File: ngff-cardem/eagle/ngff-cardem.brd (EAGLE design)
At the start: 90 x 100 mm, 150 parts, among them IC1 FPF2109, IC2 FPF2109, IC201 CB3Q3244PW, IC202 CB3Q3244PW, IC203 IP4234CZ6, IC3 TPS22958N-DGK, IC302 TPS22958N-DGN, J301 PJ-002BH-SMT-TR, M2 MENTOR_12701001, M3 MENTOR_12701001, Q201 12MHz, T1 BC847, T101 BC847, U201 IP4234CZ6, U202 AT91SAM3S-AU, U301 MIC5366-1.8YC5, X1 PINHD-2X3-SP, X102 ZX360D-B-10P(30), X2 171826-4-RA, X201 MINI-USB-SHIELD-UX60-MB-5ST, X202 2.54mm, X3 JACK2.5_SJ-2523

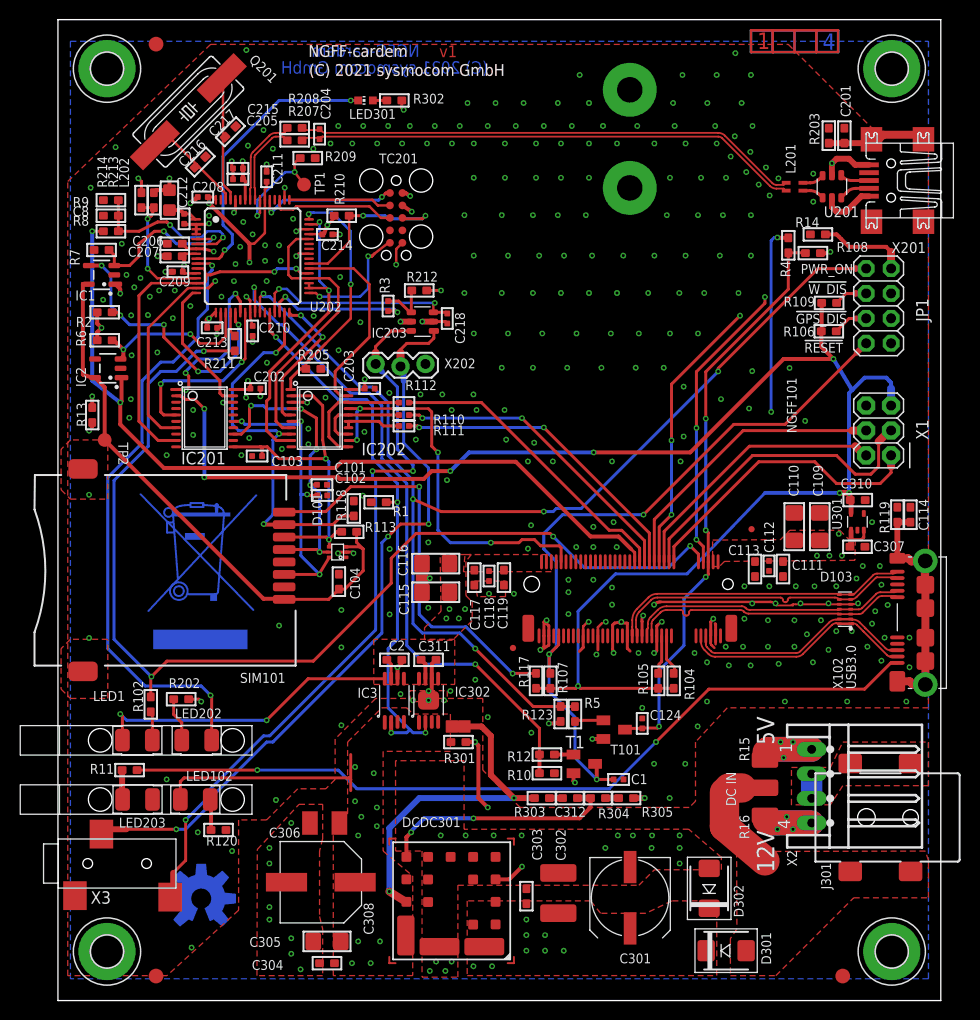
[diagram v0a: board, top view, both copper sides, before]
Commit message: ngff-cardem: run renumber-sheet.uld and normalize-texts2.ulp
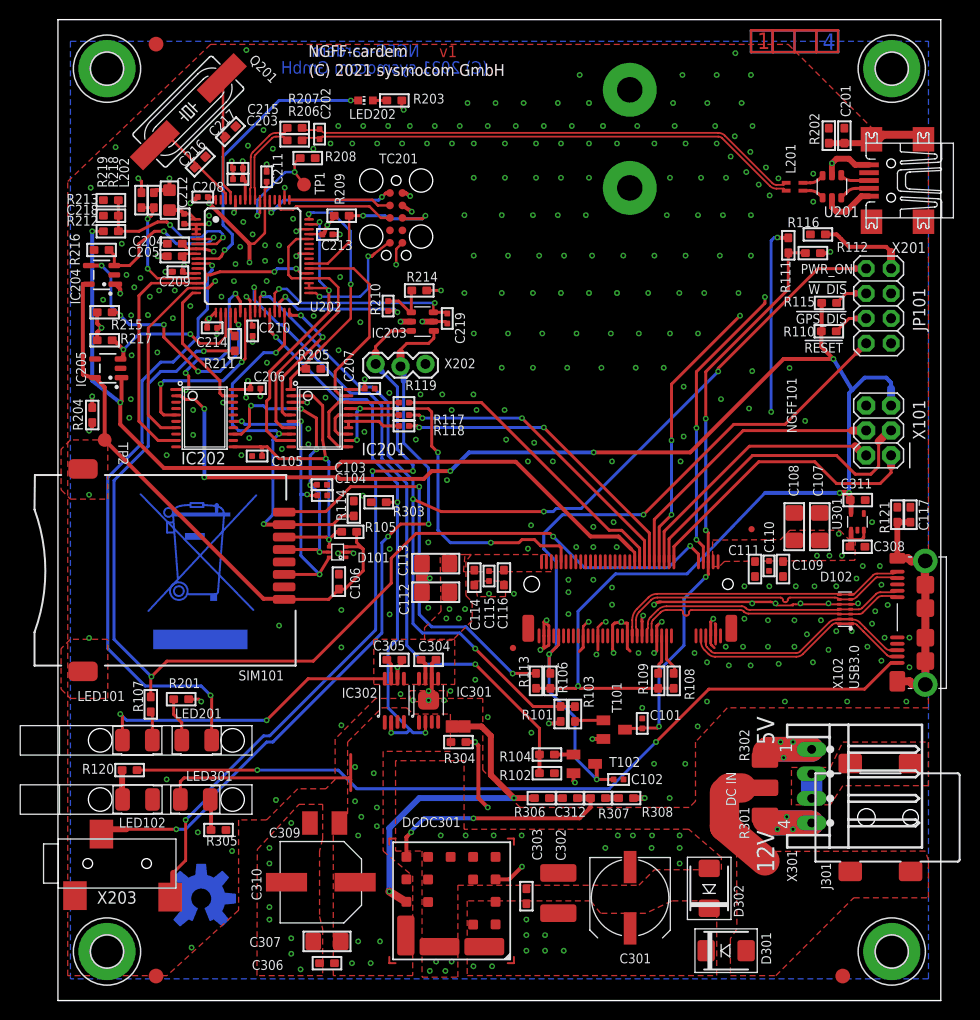
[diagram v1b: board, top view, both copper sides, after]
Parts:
- removed C1, C118, C124: 33p, rc-sysmocom:_0402
- removed C119: 10p, rc-sysmocom:_0603
- removed C2: 1n, rc-sysmocom:_0603
- removed C8, R10: DNP, rc-sysmocom:_0603
- removed H1, H2: MOUNT-PAD-ROUND3.2, holes:3,2-PAD
- removed IC3: TPS22958N-DGK, TPS22958:VSSOP8
- removed JP1: (no value), pinhead:2X04
- removed LED203: LEDPLCC2-MIN-red, LED-PLCC2:PLCC2-MIN
- removed R1, R4: 10k, rc-sysmocom:_0603
- removed R11: 510, rc-sysmocom:_0603
- removed R12: 4.7k, rc-sysmocom:_0603
- removed R15, R16: 0R, rc-sysmocom:1210
- removed R3: 47, rc-sysmocom:_0402
- removed R8: 30k, rc-sysmocom:_0603
- removed R9: 47k, rc-sysmocom:_0603
- added C105, C219: 33p, rc-sysmocom:_0402
- added C106: 100n, rc-sysmocom:_0603
- added C107, C108: 100u, rc-sysmocom:1206
- added C309: DNP, rcl:SMC_B
- added H301, H302: MOUNT-PAD-ROUND3.2, holes:3,2-PAD
- added IC301: TPS22958N-DGN, TPS22958:HVSSOP8
- added JP103: FIDUCIALUFIDUCIAL, SparkFun:MICRO-FIDUCIAL
- added LED201: LEDPLCC2-MIN-red, LED-PLCC2:PLCC2-MIN
- added R114: 47k, rc-sysmocom:_0603
- added R115, R218: 10k, rc-sysmocom:_0603
- added R121, R219: 100k, rc-sysmocom:_0603
- added R201: 330, rc-sysmocom:_0603
- added R206: 27, rc-sysmocom:_0603
- added R306: 180, rc-sysmocom:_0603
- added R307: 4.42k, rc-sysmocom:_0603
- added R308: 20, rc-sysmocom:_0603
- C104: value 100n -> 33p; device rc-sysmocom:_0603 -> rc-sysmocom:_0402
- C109: value 100u -> 100n; device rc-sysmocom:1206 -> rc-sysmocom:_0603
- C110, C115: value 100u -> 33p; device rc-sysmocom:1206 -> rc-sysmocom:_0402
- C111: value 100n -> 10p
- C112: value 33p -> 100u; device rc-sysmocom:_0402 -> rc-sysmocom:1206
- C113: value 10p -> 100u; device rc-sysmocom:_0603 -> rc-sysmocom:1206
- C116: value 100u -> 10p; device rc-sysmocom:1206 -> rc-sysmocom:_0603
- C202: value 100n -> 33p
- C204: value 33p -> 2.2u; device rc-sysmocom:_0402 -> rc-sysmocom:_0603
- C205: value 100n -> 2.2u; device rc-sysmocom:_0402 -> rc-sysmocom:_0603
- C206, C207: value 2.2u -> 100n; device rc-sysmocom:_0603 -> rc-sysmocom:_0402
- C218: value 33p -> DNP; device rc-sysmocom:_0402 -> rc-sysmocom:_0603
- C304: value 100n -> 1n
- C305: value 22u 10V -> 1n; device rc-sysmocom:1206 -> rc-sysmocom:_0603
- C306: value DNP -> 100n; device rcl:SMC_B -> rc-sysmocom:_0603
- C307: value 100n -> 22u 10V; device rc-sysmocom:_0603 -> rc-sysmocom:1206
- C308: value 330u -> 100n; device Wurth_Elektronik_Passive_Capacitors_rev15a:4.2X1.9X2.8(BXCXA) -> rc-sysmocom:_0603
- C310: value 100n -> 330u; device rc-sysmocom:_0603 -> Wurth_Elektronik_Passive_Capacitors_rev15a:4.2X1.9X2.8(BXCXA)
- C311: value 1n -> 100n
- IC302: value TPS22958N-DGN -> TPS22958N-DGK; device TPS22958:HVSSOP8 -> TPS22958:VSSOP8
- JP101: value FIDUCIALUFIDUCIAL -> (none); device SparkFun:MICRO-FIDUCIAL -> pinhead:2X04
- LED102: value LEDPLCC2-MIN -> LEDPLCC2-MIN-red
- LED202: value LEDPLCC2-MIN-red -> KPH-1608SGC; device LED-PLCC2:PLCC2-MIN -> led:CHIP-LED0603
- LED301: value KPH-1608SGC -> LEDPLCC2-MIN; device led:CHIP-LED0603 -> LED-PLCC2:PLCC2-MIN
- R102: value 330 -> DNP
- R104: value 10k -> 4.7k
- R105: value 10k -> DNP
- R107: value 10k -> 330
- R108: value 100k -> 10k
- R110, R111: value 47 -> 10k; device rc-sysmocom:_0402 -> rc-sysmocom:_0603
- R112: value 47 -> 100k; device rc-sysmocom:_0402 -> rc-sysmocom:_0603
- R113: value DNP -> 4.7k
- R117: value 4.7k -> 47; device rc-sysmocom:_0603 -> rc-sysmocom:_0402
- R118: value 47k -> 47; device rc-sysmocom:_0603 -> rc-sysmocom:_0402
- R119: value 100k -> 47; device rc-sysmocom:_0603 -> rc-sysmocom:_0402
- R120: value 330 -> 510
- R202: value 330 -> 100k
- R203: value 100k -> 330
- R208: value 27 -> 10k
- R209: value 10k -> 1.5k
- R210: value 1.5k -> 47; device rc-sysmocom:_0603 -> rc-sysmocom:_0402
- R212: value 100k -> 30k
- R213: value 10k -> 47k
- R301: value 100k -> 0R; device rc-sysmocom:_0603 -> rc-sysmocom:1210
- R302: value 330 -> 0R; device rc-sysmocom:_0603 -> rc-sysmocom:1210
- R303: value 180 -> 10k
- R304: value 4.42k -> 100k
- R305: value 20 -> 330
- moved H303 90.0 mm to (5.00, 5.00)
- moved H304 90.0 mm to (85.0, 5.00)
- moved R202 87.5 mm to (78.6, 88.2), turned to 90 degrees
- moved R302 78.3 mm to (72.1, 23.1), turned to 90 degrees
- moved LED301 73.3 mm to (14.0, 20.5), turned to 0 degrees
- moved LED202 67.4 mm to (31.4, 91.8), turned to 90 degrees
- moved C307 67.4 mm to (27.4, 6.03)
- moved C310 67.2 mm to (26.8, 12.1), turned to 0 degrees
- moved C308 64.5 mm to (81.5, 46.3), turned to 180 degrees
- moved R119 51.6 mm to (35.3, 61.0), turned to 180 degrees
- moved JP101 51.0 mm to (83.7, 70.8), turned to 270 degrees
- moved C311 46.7 mm to (81.5, 51.0)
- moved R108 45.9 mm to (62.8, 32.6), turned to 270 degrees
- moved R106 45.6 mm to (50.2, 32.6), turned to 270 degrees
- moved C114 44.9 mm to (42.4, 43.1), turned to 90 degrees
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- renumbered D103 to D102, IC1 to IC204, IC2 to IC205, LED1 to LED101, R123 to R101, R13 to R204, R14 to R116, R2 to R215, R5 to R103, R6 to R217, R7 to R216, T1 to T102, X1 to X101, X2 to X301, X3 to X203
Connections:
- net !BODY_SAR: now also R109.1; no longer R105.1
- net !CONNECT_MDM_SIM: now also IC201.1; no longer IC202.1
- net !CONNECT_UART1: now also IC202.19; no longer IC201.19
- net !CONNECT_UART2: now also IC201.19; no longer IC202.19
- net !GPS_DISABLE: now also JP101.5, R110.1; no longer JP1.5, R106.1
- net !MDM_UIM_RST: now also IC201.14, IC201.15, R118.2; no longer IC202.14, IC202.15, R111.2
- net !NGFF_RESET: now also C102.1, JP101.7, R106.1; no longer C1.1, JP1.7, R107.1
- net !PWR_ON: now also JP101.1; no longer JP1.1
- net !SET_SIM_DET: now also IC202.1; no longer IC201.1
- net !SIMTRACE_RESET: now also R209.1; no longer R210.1
- net !SLOT_RST: now also C104.1, IC201.6, IC202.15; no longer C102.1, IC201.15, IC202.6
- net !ST_UART1_RST: now also IC202.5; no longer IC201.5
- net !ST_UART2_RST: now also IC201.5; no longer IC202.5
- net !WAKE_ON_WWAN: now also R108.1; no longer R104.1
- net !W_DISABLE: now also JP101.3, R115.1; no longer JP1.3, R109.1
- net +VIN: now also R301.2, R302.1; no longer R15.1, R16.2
- net ERASE: now also R208.2; no longer R209.2
- net GND: now also C105.2, C106.2, C107.1, C108.1, C110.2, C111.2, C112.1, C113.1, C115.2, C116.2, C204.1, C219.2, C305.1, C306.1, C307.2, C308.1, C309.-, C310.2, H301.B3,2, H302.B3,2, IC301.6, IC301.EXP, JP101.4, JP101.6, JP101.8, LED102.K, R102.2, R112.1, R114.1, R121.1, R202.2, R208.1, R213.1, R219.1, R303.1, R305.1, R308.2; no longer C1.2, C110.1, C111.1, C112.2, C113.2, C115.1, C116.1, C118.2, C119.2, C124.2, C2.1, C202.1, C305.2, C306.-, C307.1, C308.2, C310.1, C8.2, H1.B3,2, H2.B3,2, IC3.6, IC302.EXP, JP1.4, JP1.6, JP1.8, LED203.K, R1.1, R10.2, R108.1, R118.1, R119.1, R120.1, R203.2, R209.1, R214.1, R305.2, R9.1
- net MDM_SIM_DET: now also IC201.12, IC201.17; no longer IC202.12, IC202.17
- net MDM_UIM_CLK: now also IC201.13, IC201.16, R117.2; no longer IC202.13, IC202.16, R110.2
- net MDM_UIM_IO: now also IC201.11, IC201.18, R119.2; no longer IC202.11, IC202.18, R112.2
- net MDM_UIM_VDD: now also R212.2; no longer R8.2
- net MODEM_EN: now also IC301.2, R303.2; no longer IC3.2, R1.2
- net N$10: now also C117.2, R121.2; no longer C114.2, R119.2
- net N$11: now also R104.1; no longer R12.1
- net N$12: now also LED201.A, R201.1; no longer LED202.A, R202.1
- net N$13: now also R304.2; no longer R301.2
- net N$18: now also C218.1, R212.1, R213.2; no longer C8.1, R8.1, R9.2
- net N$19: now also LED102.A, R120.1; no longer LED203.A, R11.1
- net N$20: now also C305.2, IC302.7; no longer C2.2, IC3.7
- net N$21: now also JP101.2; no longer JP1.2
- net N$22: now also R107.1; no longer R102.1
- net N$23: now also R301.1; no longer R16.1
- net N$24: now also R302.2; no longer R15.2
- net N$3: now also R113.2; no longer R117.2
- net N$4: now also LED202.A, R203.2; no longer LED301.A, R302.2
- net N$5: now also IC201.3, IC202.18; no longer IC201.18, IC202.3
- net N$59: now also R307.2, R308.1; no longer R304.2, R305.1
- net N$6: now also R306.2; no longer R303.2
- net N$7: now also LED301.K, R305.2; no longer LED102.K, R120.2
- net N$8: now also R210.1; no longer R3.1
- net N$9: now also R202.1; no longer R203.1
- net N$91: now also C304.2, IC301.7; no longer C311.2, IC302.7
- net NGFF_USB_VBUS: now also R120.2; no longer R11.2
- net PERST: now also R102.1, R104.2; no longer R10.1, R12.2
- net PWR_ON: now also C101.1, R111.2, R112.2; no longer C124.1, R108.2, R4.2
- net SENSE: now also R306.1; no longer R303.1
- net SIMTRACE12_USB_D_N: now also C202.1, R206.1; no longer C204.1, R207.1
- net SIMTRACE12_USB_D_P: now also C202.2, R207.1; no longer C204.2, R208.1
- net SIMTRACE_LED_GREEN: now also LED201.K; no longer LED202.K
- net SIMTRACE_LED_RED: now also LED202.C; no longer LED301.C
- net SLOT_CLK: now also C103.1, IC201.4, IC202.13; no longer C101.1, IC201.13, IC202.4
- net SLOT_DET: now also IC201.8, R114.2; no longer IC202.8, R118.2
- net SLOT_IO: now also C105.1, IC201.2, IC202.11, R105.2; no longer C103.1, IC201.11, IC202.2, R113.2
- net SLOT_VDD: now also C106.1, R105.1; no longer C104.1, R113.1
- net ST_DRXD: now also R210.2, R214.1; no longer R212.1, R3.2
- net ST_DTXD: now also C219.1; no longer C218.1
- net ST_UART1_CLK: now also IC202.7; no longer IC201.7
- net ST_UART1_IO: now also IC202.9; no longer IC201.9
- net ST_UART2_CLK: now also IC201.7; no longer IC202.7
- net ST_UART2_IO: now also IC201.9; no longer IC202.9
- net TRIM: now also R307.1; no longer R304.1
- net VCC_1V8: now also C311.2, IC202.2, R108.2, R110.2, R113.1, R115.2; no longer C310.2, IC201.2, R104.2, R105.2, R107.2, R117.1
- net VCC_3V3: now also C204.2, C207.2, C306.2, C307.1, C309.+, C310.1, IC301.1, IC301.3, IC301.4, LED301.A, R201.2, R203.1, R209.2, R214.2, R218.1, R304.1; no longer C202.2, C205.2, C304.2, C305.1, C306.+, C308.1, IC3.1, IC3.3, IC3.4, LED102.A, R202.2, R210.2, R212.2, R213.1, R301.1, R302.1
- net VDD_1V8_SIMTRACE12: now also C205.2; no longer C207.2
- net VERSION_DETECT: now also R218.2, R219.2; no longer R213.2, R214.2
- net V_MODEM: now also C107.2, C108.2, C110.1, C111.1, C112.2, C113.2, C114.2, C115.1, C116.1, C308.2, IC301.5, IC301.8, R111.1; no longer C110.2, C111.2, C112.1, C113.1, C115.2, C116.2, C117.2, C118.1, C119.1, C307.2, IC3.5, IC3.8, R4.1
- net WWAN: now also R107.2; no longer R102.2
- net _!USIM1_RESET: now also R118.1; no longer R111.1
- net _SIMTRACE12_USB_D_N: now also R206.2; no longer R207.2
- net _SIMTRACE12_USB_D_P: now also R207.2; no longer R208.2
- net _USIM1_CLK: now also R117.1; no longer R110.1
- net _USIM1_DATA: now also R119.1; no longer R112.1

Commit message: ngff-cardem: update parts for BOM (in gnumeric and xls)
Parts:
- C312: value 3300p -> 8200p
- LED102, LED201: value LEDPLCC2-MIN-red -> LEDPLCC2-MIN-green
- LED202: value KPH-1608SGC -> KPH-1608EC
- LED301: value LEDPLCC2-MIN -> LEDPLCC2-MIN-green
- R302: value 0R -> DNP

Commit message: ngff-cardem: make DCDC301 default to Murata OKL-T/3-W12P-C
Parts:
- DCDC301: value PVX003A0X3-SRZ -> OKL-T/3-W12P-C
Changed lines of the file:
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@@
 <attribute name="VALUE" x="9.7165" y="83.5024" size="0.508" layer="27" font="vector" ratio="10" rot="R270"/>
 </element>
-<element name="DCDC301" library="DC-DC_CONVERTER" package="DC-DC_CON-ALLPADS" value="PVX003A0X3-SRZ" x="40.1325" y="10.165" smashed="yes" rot="R180">
+<element name="DCDC301" library="DC-DC_CONVERTER" package="DC-DC_CON-ALLPADS" value="OKL-T/3-W12P-C" x="40.1325" y="10.165" smashed="yes" rot="R180">
 <attribute name="NAME" x="41.0525" y="18.6875" size="1" layer="25" ratio="16" rot="R180"/>
-<attribute name="DESCRIPTION" value="DC DC CONVERTER 0.6-5.5V 16.5W" x="40.1325" y="10.165" size="1.778" layer="27" rot="R180" display="off"/>
-<attribute name="MANUFACTURER" value="ABB Power Electronics Inc." x="40.1325" y="10.165" size="1.778" layer="27" rot="R180" display="off"/>
-<attribute name="MANUFACTURERPARTNUMBER" value="PVX003A0X3-SRZ" x="40.1325" y="10.165" size="1.778" layer="27" rot="R180" display="off"/>
+<attribute name="DESCRIPTION" value="DC DC CONVERTER 0.591-5.5V 15W" x="40.1325" y="10.165" size="1.778" layer="27" rot="R180" display="off"/>
+<attribute name="MANUFACTURER" value="Murata Power Solutions Inc." x="40.1325" y="10.165" size="1.778" layer="27" rot="R180" display="off"/>
+<attribute name="MANUFACTURERPARTNUMBER" value="OKL-T/3-W12P-C" x="40.1325" y="10.165" size="1.778" layer="27" rot="R180" display="off"/>
 <attribute name="SOURCE" value="DIGIKEY" x="40.1325" y="10.165" size="1.778" layer="27" rot="R180" display="off"/>
-<attribute name="SOURCEPARTNUMBER" value="555-1264-1-ND" x="40.1325" y="10.165" size="1.778" layer="27" rot="R180" display="off"/>
+<attribute name="SOURCEPARTNUMBER" value="811-2709-1-ND" x="40.1325" y="10.165" size="1.778" layer="27" rot="R180" display="off"/>
 <attribute name="ROHSCERTIFICATE" value="RoHS-konform" x="40.1325" y="10.165" size="1.778" layer="27" rot="R180" display="off"/>
 <attribute name="POPULATED" value="TRUE" x="40.1325" y="10.165" size="1.778" layer="27" rot="R180" display="off"/>
 <attribute name="CLASS" value="DC/DC CONVERTER" x="40.1325" y="10.165" size="1.778" layer="27" rot="R180" display="off"/>
-<attribute name="LINK" value="https://www.digikey.de/product-detail/de/abb-power-electronics-inc/PVX003A0X3-SRZ/555-1264-1-ND" x="40.1325" y="10.165" size="1.778" layer="27" rot="R180" display="off"/>
+<attribute name="LINK" value="https://www.digikey.de/product-detail/de/murata-power-solutions-inc/OKL-T-3-W12P-C/811-2709-1-ND" x="40.1325" y="10.165" size="1.778" layer="27" rot="R180" display="off"/>
 </element>
 <element name="R304" library="rc-sysmocom" package="_0603" value="100k" x="40.825" y="26.3525" smashed="yes">

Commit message: ngff-cardem: exchange two BJT to available types (BC850)
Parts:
- T101, T102: value BC847 -> BC850
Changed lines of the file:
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@@
 <attribute name="LINK" value="https://www.digikey.de/product-detail/de/te-connectivity-passive-product/CRG0603F10K-10/A121523CT-ND/" x="18.035" y="66.9925" size="1.778" layer="27" rot="R90" display="off"/>
 </element>
-<element name="T101" library="transistor" package="SOT23-BEC" value="BC847" x="56.705" y="27.6175" smashed="yes" rot="R270">
+<element name="T101" library="transistor" package="SOT23-BEC" value="BC850" x="56.705" y="27.6175" smashed="yes" rot="R270">
 <attribute name="NAME" x="57.4625" y="29.3375" size="1" layer="25" ratio="16" rot="R90"/>
 <attribute name="VALUE" x="53.53" y="29.5225" size="1.27" layer="27" rot="R270"/>
-<attribute name="DESCRIPTION" value="TRANS NPN 45V 0.1A SOT23" x="56.705" y="27.6175" size="1.778" layer="27" rot="R270" display="off"/>
+<attribute name="DESCRIPTION" value="TRANS NPN 45V 100MA TO236AB" x="56.705" y="27.6175" size="1.778" layer="27" rot="R270" display="off"/>
 <attribute name="MANUFACTURER" value="Nexperia USA Inc." x="56.705" y="27.6175" size="1.778" layer="27" rot="R270" display="off"/>
-<attribute name="MANUFACTURERPARTNUMBER" value="BC847C,215" x="56.705" y="27.6175" size="1.778" layer="27" rot="R270" display="off"/>
+<attribute name="MANUFACTURERPARTNUMBER" value="BC850C,235" x="56.705" y="27.6175" size="1.778" layer="27" rot="R270" display="off"/>
 <attribute name="SOURCE" value="DIGIKEY" x="56.705" y="27.6175" size="1.778" layer="27" rot="R270" display="off"/>
-<attribute name="SOURCEPARTNUMBER" value="1727-2924-1-ND" x="56.705" y="27.6175" size="1.778" layer="27" rot="R270" display="off"/>
+<attribute name="SOURCEPARTNUMBER" value="1727-6194-1-ND" x="56.705" y="27.6175" size="1.778" layer="27" rot="R270" display="off"/>
 <attribute name="ROHSCERTIFICATE" value="RoHS3-konform" x="56.705" y="27.6175" size="1.778" layer="27" rot="R270" display="off"/>
 <attribute name="POPULATED" value="TRUE" x="56.705" y="27.6175" size="1.778" layer="27" rot="R270" display="off"/>
 <attribute name="CLASS" value="TRANSISTOR" x="56.705" y="27.6175" size="1.778" layer="27" rot="R270" display="off"/>
-<attribute name="LINK" value="https://www.digikey.de/product-detail/de/nexperia-usa-inc/BC847C,215/1727-2924-1-ND" x="56.705" y="27.6175" size="1.778" layer="27" rot="R270" display="off"/>
+<attribute name="LINK" value="https://www.digikey.de/product-detail/de/nexperia-usa-inc/BC850C-235/1727-6194-1-ND/" x="56.705" y="27.6175" size="1.778" layer="27" rot="R270" display="off"/>
 </element>
 <element name="C101" library="rc-sysmocom" package="_0402" value="33p" x="59.5625" y="28.2525" smashed="yes" rot="R90">
@@
 <attribute name="VALUE" x="34.9886" y="69.5325" size="0.508" layer="27" font="vector" ratio="10" rot="R90"/>
 </element>
-<element name="T102" library="transistor" package="SOT23-BEC" value="BC847" x="53.6575" y="24.13" smashed="yes" rot="R270">
-<attribute name="SOURCEPARTNUMBER" value="1727-2924-1-ND" x="53.6575" y="24.13" size="1.016" layer="27" ratio="14" rot="R270" display="off"/>
-<attribute name="DESCRIPTION" value="TRANS NPN 45V 0.1A SOT23" x="53.6575" y="24.13" size="1.016" layer="27" ratio="14" rot="R270" display="off"/>
-<attribute name="CLASS" value="TRANSISTOR" x="53.6575" y="24.13" size="1.016" layer="27" ratio="14" rot="R270" display="off"/>
-<attribute name="SOURCE" value="DIGIKEY" x="53.6575" y="24.13" size="1.016" layer="27" ratio="14" rot="R270" display="off"/>
-<attribute name="LINK" value="https://www.digikey.de/product-detail/de/nexperia-usa-inc/BC847C,215/1727-2924-1-ND" x="53.6575" y="24.13" size="1.016" layer="27" ratio="14" rot="R270" display="off"/>
-<attribute name="MANUFACTURER" value="Nexperia USA Inc." x="53.6575" y="24.13" size="1.016" layer="27" ratio="14" rot="R270" display="off"/>
-<attribute name="MANUFACTURERPARTNUMBER" value="BC847C,215" x="53.6575" y="24.13" size="1.016" layer="27" ratio="14" rot="R270" display="off"/>
-<attribute name="POPULATED" value="TRUE" x="53.6575" y="24.13" size="1.016" layer="27" ratio="14" rot="R270" display="off"/>
-<attribute name="ROHSCERTIFICATE" value="RoHS3-konform" x="53.6575" y="24.13" size="1.016" layer="27" ratio="14" rot="R270" display="off"/>
+<element name="T102" library="transistor" package="SOT23-BEC" value="BC850" x="53.6575" y="24.13" smashed="yes" rot="R270">
 <attribute name="NAME" x="56.1975" y="23.8125" size="1.016" layer="25" ratio="14"/>
 <attribute name="VALUE" x="50.4825" y="26.035" size="1.27" layer="27" rot="R270"/>
+<attribute name="DESCRIPTION" value="TRANS NPN 45V 100MA TO236AB" x="53.6575" y="24.13" size="1.778" layer="27" rot="R270" display="off"/>
+<attribute name="MANUFACTURER" value="Nexperia USA Inc." x="53.6575" y="24.13" size="1.778" layer="27" rot="R270" display="off"/>
+<attribute name="MANUFACTURERPARTNUMBER" value="BC850C,235" x="53.6575" y="24.13" size="1.778" layer="27" rot="R270" display="off"/>
+<attribute name="SOURCE" value="DIGIKEY" x="53.6575" y="24.13" size="1.778" layer="27" rot="R270" display="off"/>
+<attribute name="SOURCEPARTNUMBER" value="1727-6194-1-ND" x="53.6575" y="24.13" size="1.778" layer="27" rot="R270" display="off"/>
+<attribute name="ROHSCERTIFICATE" value="RoHS3-konform" x="53.6575" y="24.13" size="1.778" layer="27" rot="R270" display="off"/>
+<attribute name="POPULATED" value="TRUE" x="53.6575" y="24.13" size="1.778" layer="27" rot="R270" display="off"/>
+<attribute name="CLASS" value="TRANSISTOR" x="53.6575" y="24.13" size="1.778" layer="27" rot="R270" display="off"/>
+<attribute name="LINK" value="https://www.digikey.de/product-detail/de/nexperia-usa-inc/BC850C-235/1727-6194-1-ND/" x="53.6575" y="24.13" size="1.778" layer="27" rot="R270" display="off"/>
 </element>
 <element name="C102" library="rc-sysmocom" package="_0402" value="33p" x="57.15" y="22.5425" smashed="yes">

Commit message: ngff-cardem: populate R102 to uncond' release /NGFF_RESET (solves SYS#5531)
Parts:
- R102: value DNP -> 10k
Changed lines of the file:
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@@
 <attribute name="VALUE" x="55.88" y="21.2089" size="0.508" layer="27" font="vector" ratio="10"/>
 </element>
-<element name="R102" library="rc-sysmocom" package="_0603" value="DNP" x="49.8475" y="23.1775" smashed="yes">
+<element name="R102" library="rc-sysmocom" package="_0603" value="10k" x="49.8475" y="23.1775" smashed="yes">
 <attribute name="NAME" x="48.26" y="23.495" size="1.016" layer="25" font="vector" ratio="14" rot="R180"/>
 <attribute name="VALUE" x="48.26" y="21.6852" size="0.508" layer="27" font="vector" ratio="10"/>
-<attribute name="DESCRIPTION" value="NO DESCRIPTION" x="49.8475" y="23.1775" size="1.778" layer="27" display="off"/>
-<attribute name="MANUFACTURER" value="UNKNOWN MANUFACTURER" x="49.8475" y="23.1775" size="1.778" layer="27" display="off"/>
-<attribute name="MANUFACTURERPARTNUMBER" value="UNKNOWN MANUFACTURER PART NUMBER" x="49.8475" y="23.1775" size="1.778" layer="27" display="off"/>
-<attribute name="SOURCE" value="UNKNOWN SOURCE" x="49.8475" y="23.1775" size="1.778" layer="27" display="off"/>
-<attribute name="SOURCEPARTNUMBER" value="UNKNOWN SOURCE PART NUMBER" x="49.8475" y="23.1775" size="1.778" layer="27" display="off"/>
-<attribute name="ROHSCERTIFICATE" value="UNKNOWN ROHS CERTIFICATE" x="49.8475" y="23.1775" size="1.778" layer="27" display="off"/>
-<attribute name="POPULATED" value="FALSE" x="49.8475" y="23.1775" size="1.778" layer="27" display="off"/>
+<attribute name="DESCRIPTION" value="RES SMD 10K OHM 1%% 1/10W 0603" x="49.8475" y="23.1775" size="1.778" layer="27" display="off"/>
+<attribute name="MANUFACTURER" value="TE Connectivity Passive Product" x="49.8475" y="23.1775" size="1.778" layer="27" display="off"/>
+<attribute name="MANUFACTURERPARTNUMBER" value="CRG0603F10K/10" x="49.8475" y="23.1775" size="1.778" layer="27" display="off"/>
+<attribute name="SOURCE" value="DIGIKEY" x="49.8475" y="23.1775" size="1.778" layer="27" display="off"/>
+<attribute name="SOURCEPARTNUMBER" value="A121523CT-ND" x="49.8475" y="23.1775" size="1.778" layer="27" display="off"/>
+<attribute name="ROHSCERTIFICATE" value="RoHS3-konform" x="49.8475" y="23.1775" size="1.778" layer="27" display="off"/>
+<attribute name="POPULATED" value="TRUE" x="49.8475" y="23.1775" size="1.778" layer="27" display="off"/>
 <attribute name="CLASS" value="RESISTOR" x="49.8475" y="23.1775" size="1.778" layer="27" display="off"/>
-<attribute name="LINK" value="UNKNOWN LINK" x="49.8475" y="23.1775" size="1.778" layer="27" display="off"/>
+<attribute name="LINK" value="https://www.digikey.de/product-detail/de/te-connectivity-passive-product/CRG0603F10K-10/A121523CT-ND/" x="49.8475" y="23.1775" size="1.778" layer="27" display="off"/>
 </element>
 <element name="R104" library="rc-sysmocom" package="_0603" value="4.7k" x="49.8475" y="25.0825" smashed="yes" rot="R180">
